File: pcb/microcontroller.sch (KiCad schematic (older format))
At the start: 10 parts

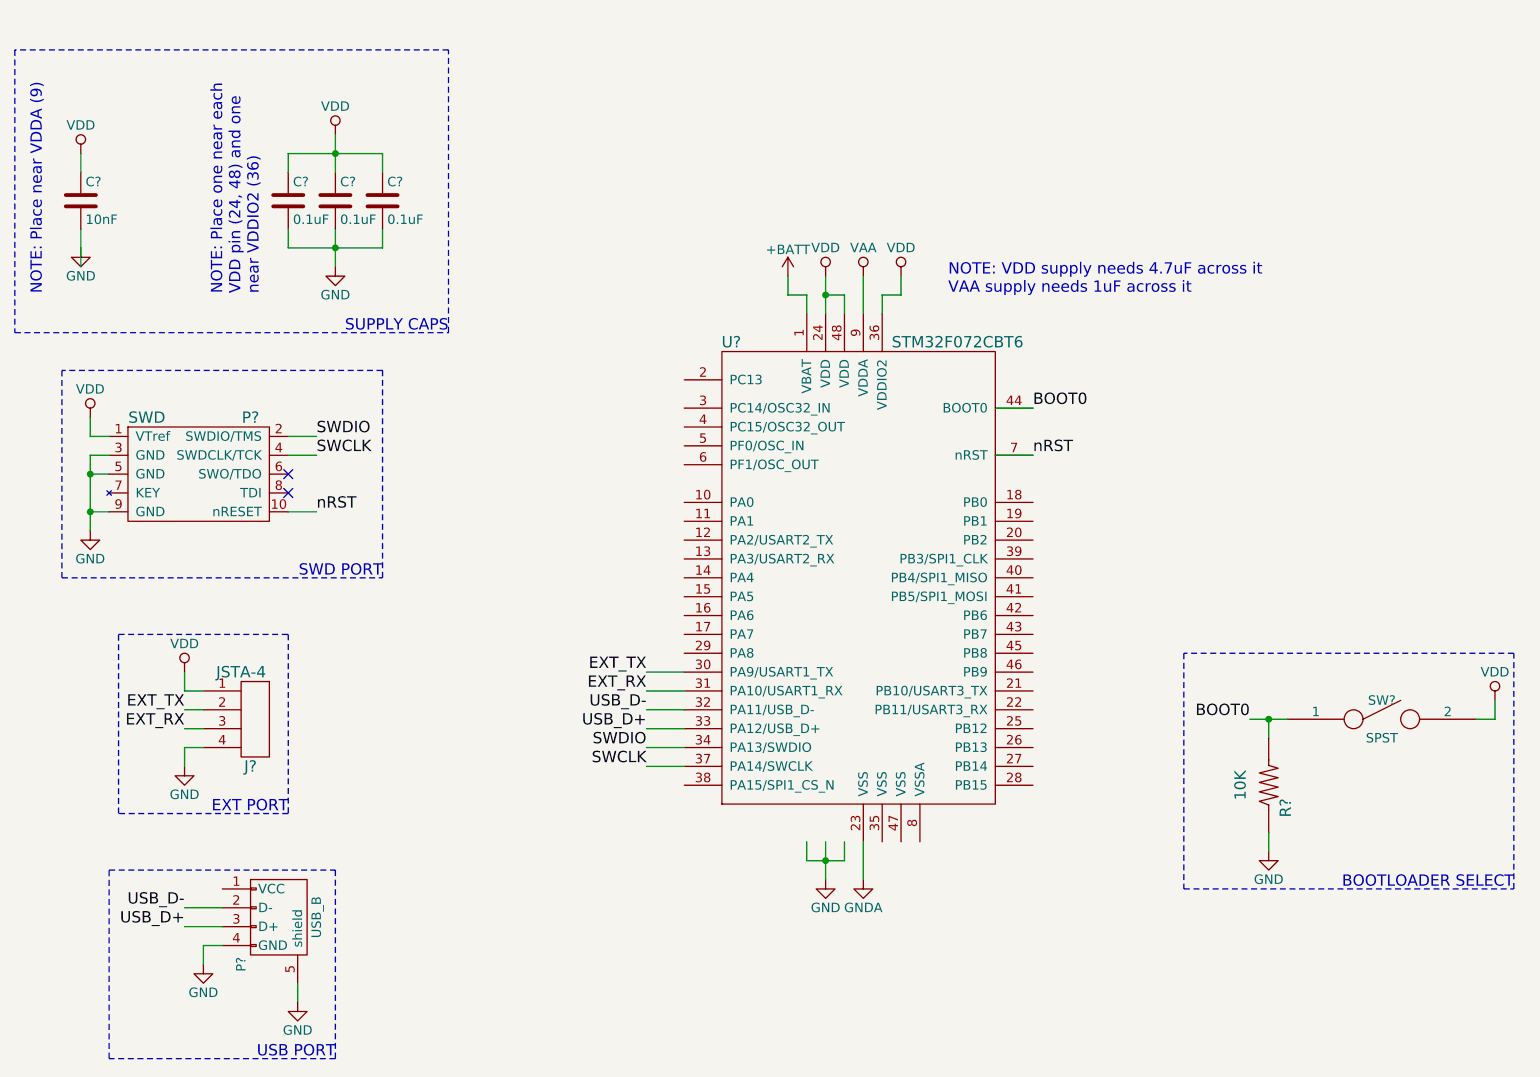
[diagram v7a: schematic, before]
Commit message: Modify pin assignments of MCU
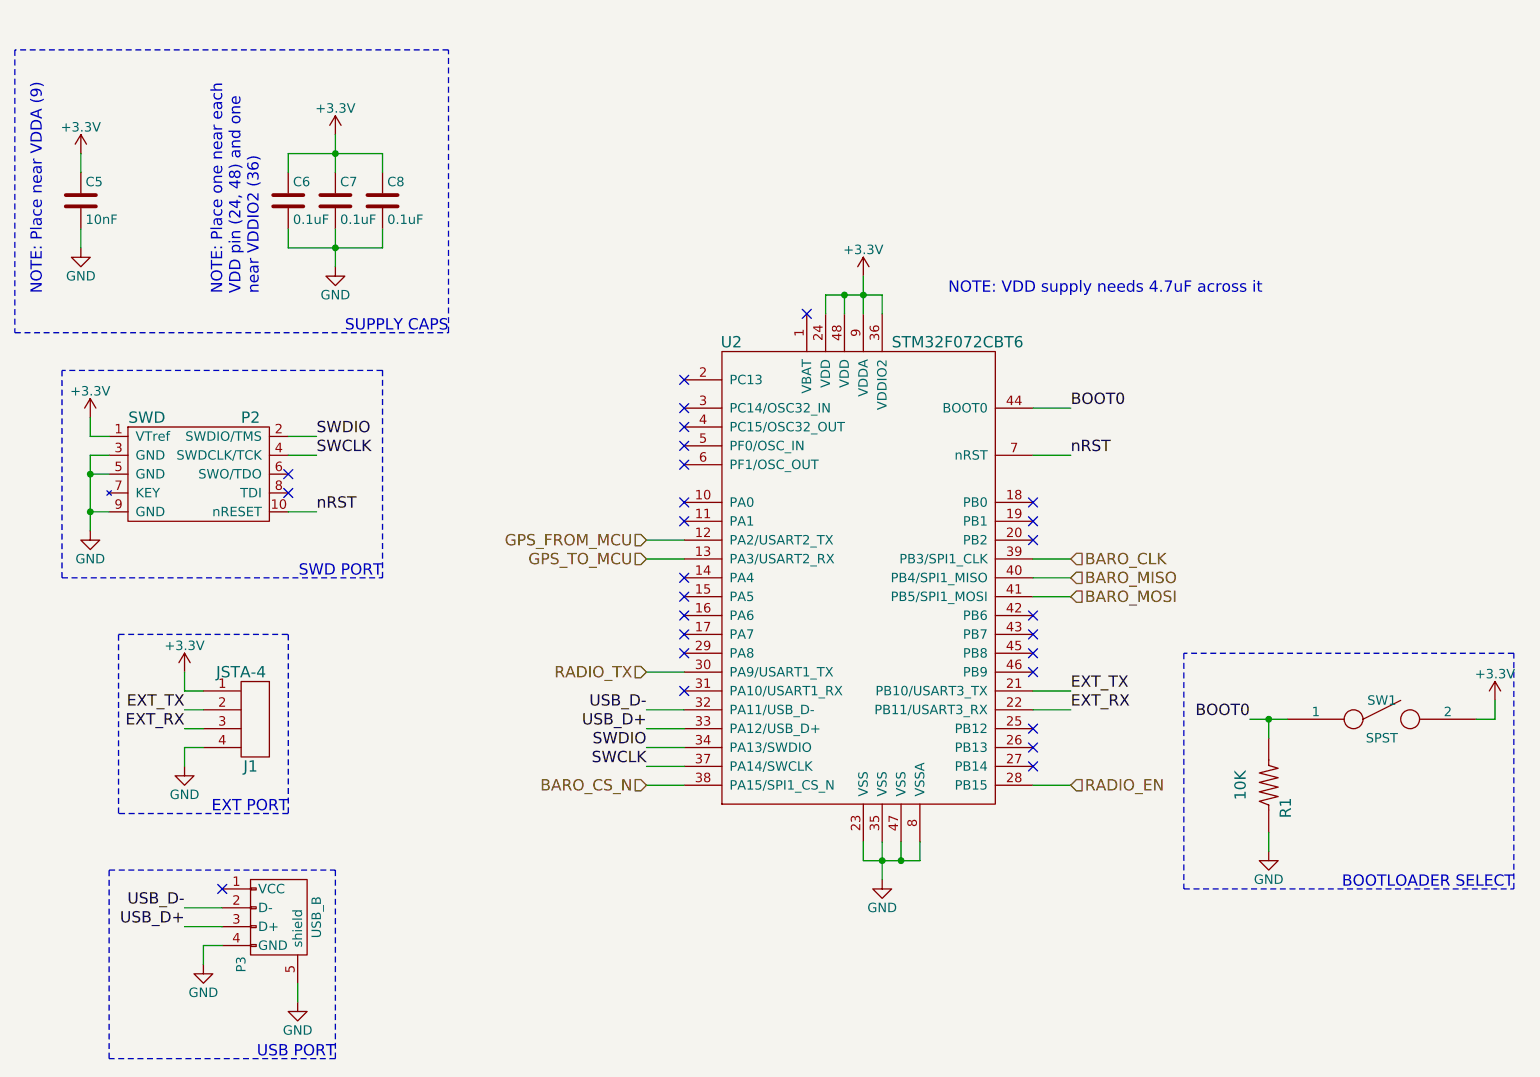
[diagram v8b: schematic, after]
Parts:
- gave numbers to parts that had none: 10
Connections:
- net labels added: +3.3V, BARO_CLK, BARO_CS_N, BARO_MISO, BARO_MOSI, GPS_FROM_MCU, GPS_TO_MCU, RADIO_EN, RADIO_TX
- net labels removed: +BATT, GNDA, VAA, VDD
- wire segments 58 -> 61
- no-connect marks 2 -> 27
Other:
- note added: "NOTE: VDD supply needs 4.7uF across it"
- note removed: "NOTE: VDD supply needs 4.7uF across it\nVAA supply needs 1uF across it"
